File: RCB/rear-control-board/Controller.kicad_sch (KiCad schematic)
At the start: 25 parts, among them J6 Conn_01x05, U1 STM32F413CGUx, U2 LD1117S33TR_SOT223, U4 MCP2551-I-SN, Y1 Crystal

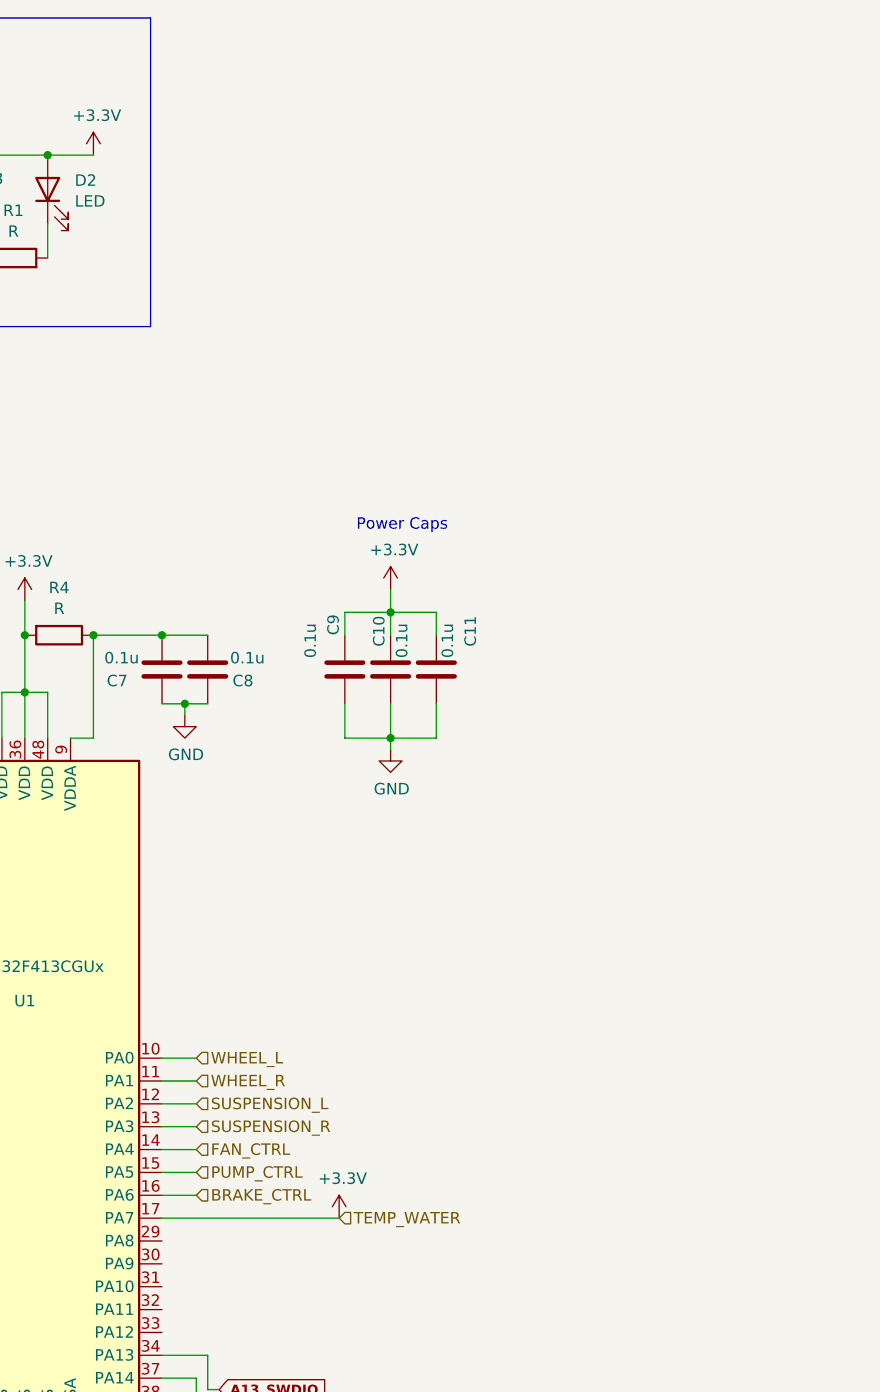
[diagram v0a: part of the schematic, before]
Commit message: working on layout
Updating traces for RCB and organizing HVB
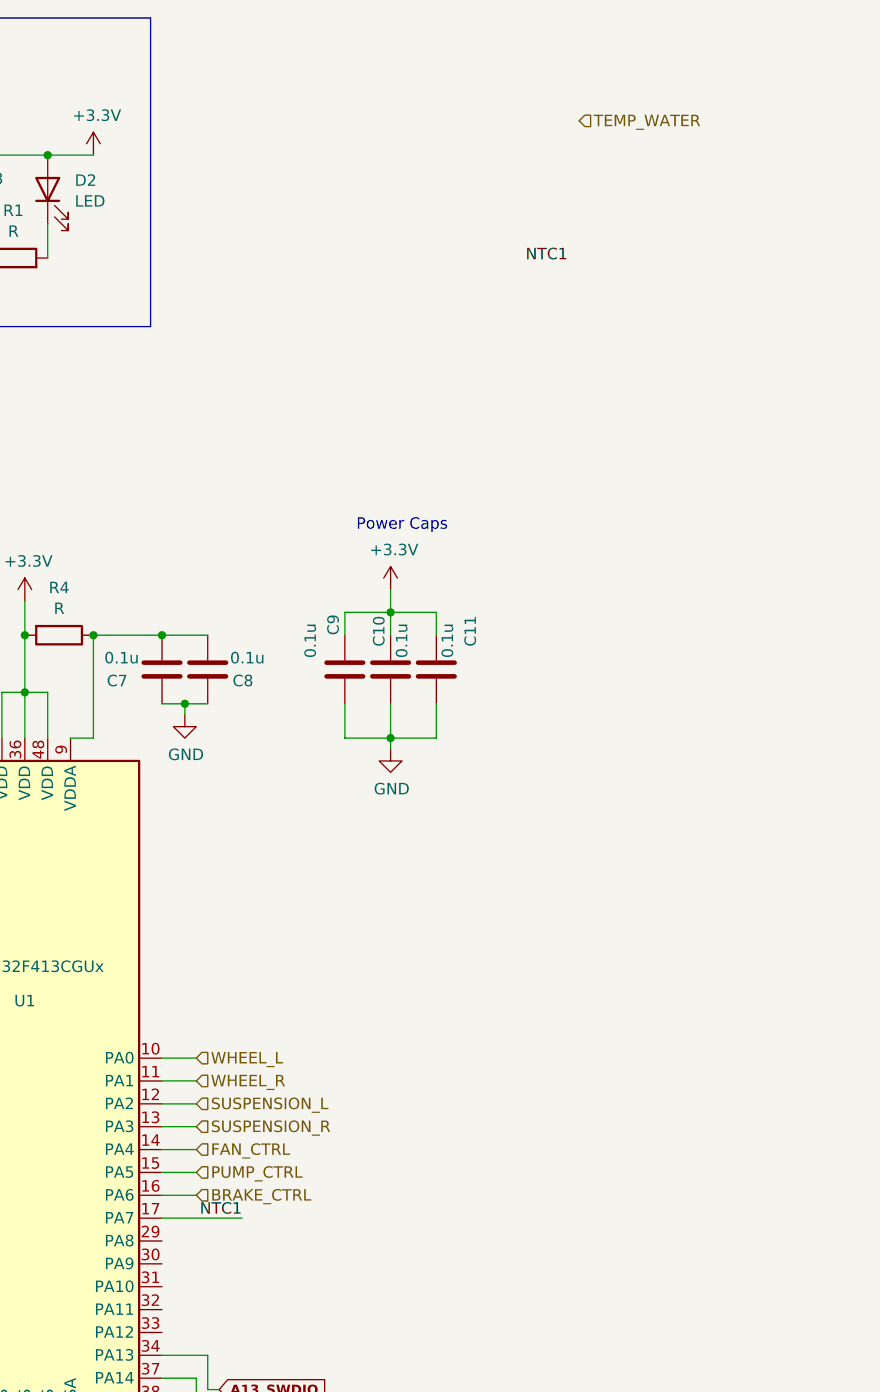
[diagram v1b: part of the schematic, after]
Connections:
- net +3V3: no longer U1.17 (PA7)
- new net NTC1: U1.17 (PA7)
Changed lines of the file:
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@@
     (stroke (width 0) (type default) (color 0 0 0 0))
   )
-  (wire (pts (xy 97.79 147.32) (xy 117.475 147.32))
+  (wire (pts (xy 97.79 147.32) (xy 106.68 147.32))
     (stroke (width 0) (type default) (color 0 0 0 0))
   )
@@
     (effects (font (size 1.27 1.27)) (justify left bottom))
   )
+  (label "NTC1" (at 142.875 41.275 180)
+    (effects (font (size 1.27 1.27)) (justify right bottom))
+  )
   (label "CAN_RX_N" (at 229.235 138.43 0)
     (effects (font (size 1.27 1.27)) (justify left bottom))
+  )
+  (label "NTC1" (at 106.68 147.32 180)
+    (effects (font (size 1.27 1.27)) (justify right bottom))
   )
   (global_label "B3_TRACESWO" (shape input) (at 238.76 48.26 180) (fields_autoplaced)
@@
     (effects (font (size 1.27 1.27)) (justify left))
   )
-  (hierarchical_label "TEMP_WATER" (shape input) (at 117.475 147.32 0)
-    (effects (font (size 1.27 1.27)) (justify left))
-  )
   (hierarchical_label "PUMP_CTRL" (shape input) (at 101.6 142.24 0)
     (effects (font (size 1.27 1.27)) (justify left))
@@
   )
   (hierarchical_label "WHEEL_R" (shape input) (at 101.6 132.08 0)
+    (effects (font (size 1.27 1.27)) (justify left))
+  )
+  (hierarchical_label "TEMP_WATER" (shape input) (at 144.145 25.4 0)
     (effects (font (size 1.27 1.27)) (justify left))
   )
@@
       (effects (font (size 1.27 1.27)) hide)
     )
-    (pin "1")
-  )
-  (symbol (lib_id "power:+3.3V") (at 117.475 147.32 0) (unit 1)
-    (in_bom yes) (on_board yes)
-    (property "Reference" "#PWR0137" (id 0) (at 117.475 151.13 0)
-      (effects (font (size 1.27 1.27)) hide)
-    )
-    (property "Value" "+3.3V" (id 1) (at 117.856 142.9258 0))
-    (property "Footprint" "" (id 2) (at 117.475 147.32 0)
-      (effects (font (size 1.27 1.27)) hide)
-    )
-    (property "Datasheet" "" (id 3) (at 117.475 147.32 0)
-      (effects (font (size 1.27 1.27)) hide)
-    )

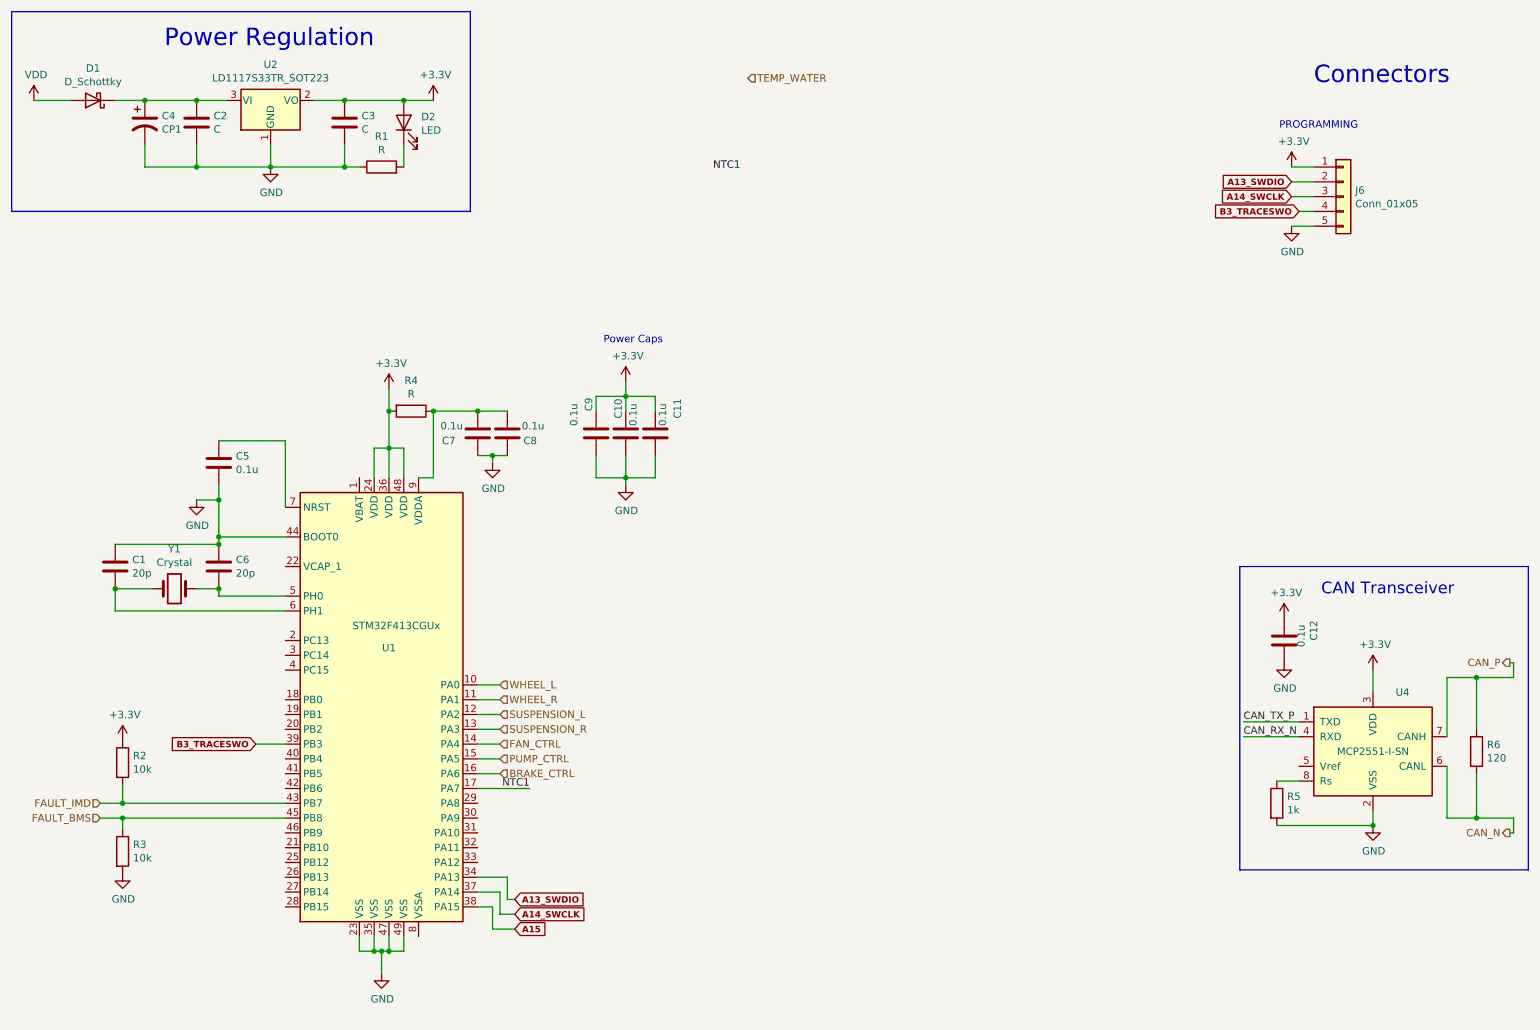
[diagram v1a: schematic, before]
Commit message: finishing layout placement
Still need to route wires
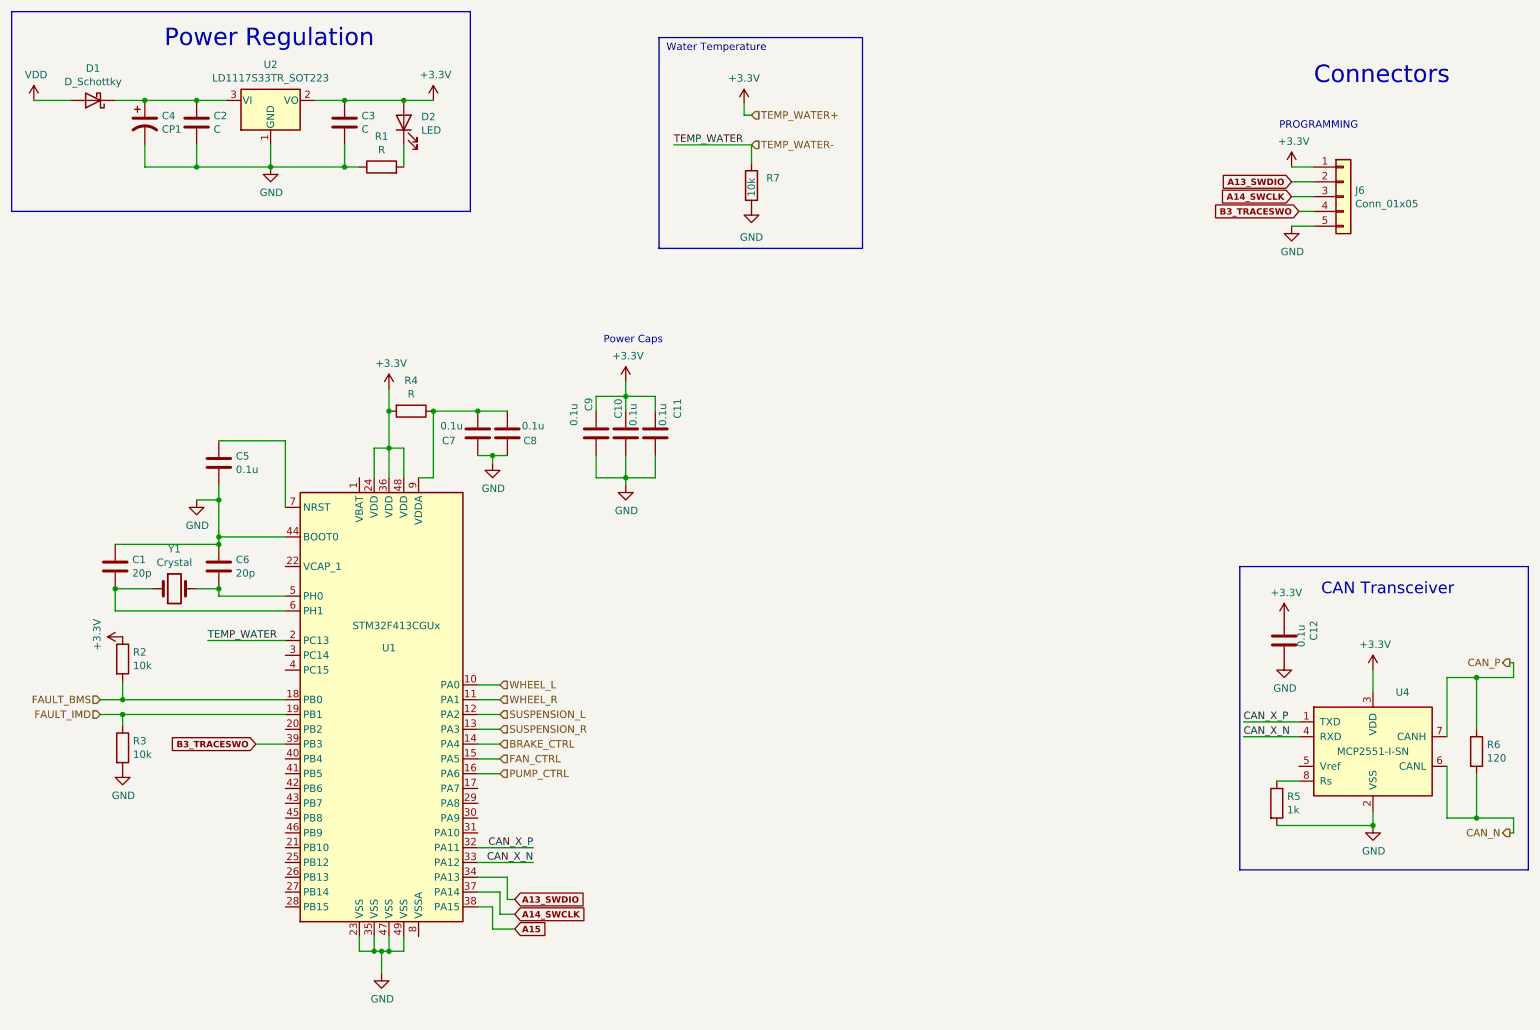
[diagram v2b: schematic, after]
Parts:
- added R7: 10k, Resistor_SMD:R_0603_1608Metric_Pad0.98x0.95mm_HandSolder, symbol Device:R
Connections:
- net CAN_RX_N is gone; now on net CAN_X_N: U4.4 (RXD)
- net CAN_TX_P is gone; now on net CAN_X_P: U4.1 (TXD)
- net BRAKE_CTRL: now also U1.14 (PA4); no longer U1.16 (PA6)
- net FAN_CTRL: now also U1.15 (PA5); no longer U1.14 (PA4)
- net FAULT_BMS: now also R2.2, U1.18 (PB0); no longer R3.1, U1.45 (PB8)
- net FAULT_IMD: now also R3.1, U1.19 (PB1); no longer R2.2, U1.43 (PB7)
- net GND: now also R7.2
- net PUMP_CTRL: now also U1.16 (PA6); no longer U1.15 (PA5)
- net TEMP_WATER-: now reaches U1.2 (PC13)
- net TEMP_WATER-: now also R7.1
- net CAN_X_P: now reaches U1.32 (PA11)
- net CAN_X_N: now reaches U1.33 (PA12)
- net NTC1: no longer names the net of U1.17 (PA7)
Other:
- note added: "Water Temperature"
- moved on the sheet: R2, R3

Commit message: trace layout complete (need review)
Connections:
- net FAN_CTRL: now also U1.16 (PA6); no longer U1.15 (PA5)
- net FAULT_BMS: now also R3.1, U1.19 (PB1); no longer R2.2, U1.18 (PB0)
- net FAULT_IMD: now also R2.2, U1.18 (PB0); no longer R3.1, U1.19 (PB1)
- net PUMP_CTRL: now also U1.15 (PA5); no longer U1.16 (PA6)
- net A15: no longer names the net of U1.38 (PA15)
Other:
- note added: "IMD is low when clear, pull high BMS is high when clear, pull low"
- moved on the sheet: C1, C10, C11, C5, C6, C7, C8, C9, R2, R3, R4, U1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

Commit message: adding mounting holes
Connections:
- net TEMP_WATER-: now also U1.17 (PA7); no longer U1.2 (PC13)
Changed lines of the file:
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@@
     (stroke (width 0) (type default) (color 0 0 0 0))
   )
-  (wire (pts (xy 107.95 123.825) (xy 94.615 123.825))
+  (wire (pts (xy 140.97 149.225) (xy 154.305 149.225))
     (stroke (width 0) (type default) (color 0 0 0 0))
   )
@@
     (effects (font (size 1.27 1.27)) (justify left bottom))
   )
-  (label "TEMP_WATER" (at 94.615 123.825 0)
-    (effects (font (size 1.27 1.27)) (justify left bottom))
+  (label "TEMP_WATER" (at 154.305 149.225 180)
+    (effects (font (size 1.27 1.27)) (justify right bottom))
   )
   (label "CAN_X_P" (at 150.495 159.385 180)
